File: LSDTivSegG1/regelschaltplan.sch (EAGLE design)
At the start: 47 parts, among them IC3 MAX232, IC4 MEGA32-P, Q2 BSS101, Q3 BSS101, Q4 BSS101, Q5 BSS101, Q6 BSS101, Q7 BSS101, Q8 BSS101, Q9 BSS101

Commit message: edit new schaltplan
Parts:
- removed IC3/7803: (no value), v-reg:78XXS
- added C12, C13, C14, C15, C16, C17: 100n, rcl:C-EU025-025X050
- added IC1: LF33AB, lsd2016:LF33AB
- added JP1: (no value), jumper:JP1E
- added R10: 10K, rcl:R-EU_0207/7
- added R11: 10k, rcl:R-EU_0207/7
- added R12, R13, R14: 240, rcl:R-EU_0207/7
- added SJ1, SJ2, SJ3, SJ4, SJ5, SJ6, SJ7, SJ8: (no value), jumper:SJ
- added SV1: (no value), con-lstb:MA05-2
- C1, C2: value (none) -> 15p
- C10, C11, C8, C9: value (none) -> 1u
- C3, C4, C6, C7: value (none) -> 100n
- C5: value (none) -> 1000u
- R1, R2, R3, R4, R5, R6, R7, R8: value (none) -> 240; device rcl:R-EU_0204/7 -> rcl:R-EU_0207/7
- R9: value (none) -> 10K; device rcl:R-EU_0204/7 -> rcl:R-EU_0207/7
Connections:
- new net ACCEL_X: C16.1, IC4.(ADC4)PA4, U$3.ACCEL_X
- new net ACCEL_Y: C17.1, IC4.(ADC3)PA3, U$3.ACCEL_Y
- new net FOOT_SW_B: IC4.(TOSC2)PC7, R11.2, U$2.FOOT_SW_B
- new net GYRO_REF: C15.1, IC4.(ADC5)PA5, U$3.GYRO_REF
- new net GYRO_X: C13.1, IC4.(ADC7)PA7, U$3.GYRO_X
- new net GYRO_Y: C14.1, IC4.(ADC6)PA6, U$3.GYRO_Y
- new net MISO: IC4.(MISO)PB6, SV1.9
- new net MOSI: IC4.(MOSI)PB5, SV1.1
- new net N$19: Q9.D, SJ8.1
- new net N$30: Q8.D, SJ7.1
- new net N$31: Q7.D, SJ6.1
- new net N$34: Q4.D, SJ3.1
- new net N$35: Q3.D, SJ2.1
- new net N$45: JP1.2, X1.9
- new net N$46: LED1.C, R3.1
- new net N$47: C5.1, IC4.(OC2)PD7, R10.1
- new net POTI: C12.1, IC4.(ADC1)PA1, U$2.POTI_CONTACT
- new net RESET: C6.2, IC4.RESET, R9.2, SV1.5
- new net SCK: IC4.(SCK)PB7, SV1.7
- new net STATUS_LED1: IC4.(T1)PB1, LED1.A
- new net STATUS_LED2: IC4.(AIN0/INT2)PB2, LED2.A
- new net STATUS_LED3: IC4.(AIN1/OC0)PB3, LED3.A
- net +3V3: now also IC1.OUT, Q9.G; no longer IC3/7803.OUT
- net +5V: now also IC1.IN, JP1.1, Q8.G, SJ1.2, SJ2.2, SJ3.2, SJ4.2, SJ5.2, SJ6.2, SJ7.2, SJ8.2, SV1.2; no longer IC3/7803.IN, Q2.D, Q3.D, Q4.D, Q5.D, Q6.D, Q7.D, Q8.D, Q9.D, X1.9
- net BAT_PWM: now also Q7.G, R10.2
- net DIROUT_1: now also IC4.(ICP)PD6, Q4.G
- net DIROUT_2: now also IC4.(INT1)PD3, Q5.G
- net ENABLE: now also IC4.(TCK)PC2, IC4.(TDO)PC4, Q6.G
- net GND: now also C12.2, C13.2, C14.2, C15.2, C16.2, C17.2, C5.2, IC1.GND, R1.2, R11.1, R12.2, R13.2, R14.2, R2.2, R3.2, R4.2, R5.2, R6.2, R7.2, R8.2, SV1.10, SV1.4, SV1.6, SV1.8; no longer IC3/7803.GND, LED1.C, LED2.C, LED3.C, R1.1, R2.1, R3.1, R4.1, R5.1, R6.1, R7.1, R8.1
- net MOTOR_PWM1: now also IC4.(OC1A)PD5, Q2.G
- net MOTOR_PWM2: now also IC4.(OC1B)PD4, Q3.G
- net N$10: now also R5.1; no longer R2.2
- net N$11: now also R6.1; no longer R3.2
- net N$14: now also R7.1; no longer R4.2
- net N$15: now also R8.1; no longer R5.2
- net N$16: now also R12.1; no longer R6.2
- net N$17: now also R13.1; no longer R7.2
- net N$18: now also R14.1; no longer R8.2
- net N$28: now also LED2.C, R2.1; no longer U$2.FOOT_SW_B
- net N$29: now also LED3.C, R1.1; no longer U$2.POTI_CONTACT
- net N$32: now also Q6.D, SJ5.1; no longer X1.3
- net N$33: now also Q5.D, SJ4.1; no longer X1.4
- net N$4: now also Q2.D, SJ1.1; no longer C6.2, IC4.RESET
- net N$7: now also R4.1; no longer R1.2
- net RS232RX: now also X1.3
- net RS232TX: now also X1.4
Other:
- moved on the sheet: C5, LEISTUNG-10, LEISTUNG-2, LEISTUNG-4, LEISTUNG-6, LEISTUNG-8, Q2, Q4, Q6, Q8, R1, R2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

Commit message: moved decoupling to regelungsplatine
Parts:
- added DC1: TMR, traco_tmr:TMR
- added IC10, IC11: LTV844, lsd2016:LTV844
- added LED12: blau, led:LED3MM
- added R15, R16, R17, R25, R26, R27: 220, rcl:R-EU_0207/10
- added R28, R29, R30, R31, R32, R33: 10k, rcl:R-EU_0207/10
- added R34: 100, rcl:R-EU_0207/10
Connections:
- net N$13 renamed NC
- removed net BAT_PWM: LEISTUNG-6.S, Q7.G, R10.2
- removed net DIROUT_1: IC4.(ICP)PD6, LEISTUNG-5.S, Q4.G
- removed net DIROUT_2: IC4.(INT1)PD3, LEISTUNG-7.S, Q5.G
- removed net ENABLE: IC4.(TCK)PC2, IC4.(TDO)PC4, LEISTUNG-9.S, Q6.G
- removed net MOTOR_PWM1: IC4.(OC1A)PD5, LEISTUNG-2.S, Q2.G
- removed net MOTOR_PWM2: IC4.(OC1B)PD4, LEISTUNG-4.S, Q3.G
- removed net N$12: LEISTUNG-8.S
- new net +24V: DC1.+VIN, LEISTUNG-1.S
- new net 5V_LST: LEISTUNG-8.S, R28.1, R29.1, R30.1, R32.1, R33.1
- new net BAT_-: DC1.-VIN, IC10G$1.EMIT, IC10G$2.EMIT, IC10G$3.EMIT, IC10G$4.C, IC11G$1.EMIT, IC11G$2.EMIT, LEISTUNG-3.S
- new net BAT_PWM_CTL: IC10G$4.COL, Q7.G, R10.2, R31.2
- new net BAT_PWM_LST: LEISTUNG-6.S, R25.1
- new net DIRL_CTL: IC4.(ICP)PD6, Q4.G, R15.1
- new net DIRL_LST: IC10G$1.COL, LEISTUNG-5.S, R28.2
- new net DIRR_CTL: IC4.(INT1)PD3, Q5.G, R16.1
- new net DIRR_LST: IC10G$2.COL, LEISTUNG-7.S, R29.2
- new net ENABLE_CTL: IC4.(TCK)PC2, IC4.(TDO)PC4, Q6.G, R17.1
- new net ENABLE_LST: IC10G$3.COL, LEISTUNG-9.S, R30.2
- new net MOTOR_PWM_LST: LEISTUNG-2.S, LEISTUNG-4.S
- new net MOTOR_PWM_L_CTL: IC4.(OC1A)PD5, Q2.G, R26.1
- new net MOTOR_PWM_L_LST: IC11G$1.COL, R32.2
- new net MOTOR_PWM_R_CTL: IC4.(OC1B)PD4, Q3.G, R27.1
- new net MOTOR_PWM_R_LST: IC11G$2.COL, R33.2
- new net N$36: IC10G$1.A, R15.2
- new net N$37: IC10G$2.A, R16.2
- new net N$38: IC10G$3.A, R17.2
- new net N$39: IC10G$4.A, R25.2
- new net N$40: IC11G$2.A, R27.2
- new net N$41: IC11G$1.A, R26.2
- new net N$42: LED12.A, R34.1
- net +5V: now also DC1.+VOUT, R31.1, R34.2; no longer LEISTUNG-1.S
- net GND: now also C11.+, DC1.-VOUT, IC10G$1.C, IC10G$2.C, IC10G$3.C, IC10G$4.EMIT, IC11G$1.C, IC11G$2.C, LED12.C; no longer C11.-, LEISTUNG-3.S
- net N$9: now also C11.-; no longer C11.+
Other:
- note added: "CTL"
- note added: "DCDC Converter"
- note added: "LST"
- note added: "On/Off NC for On State"
- note added: "Optocouplers"

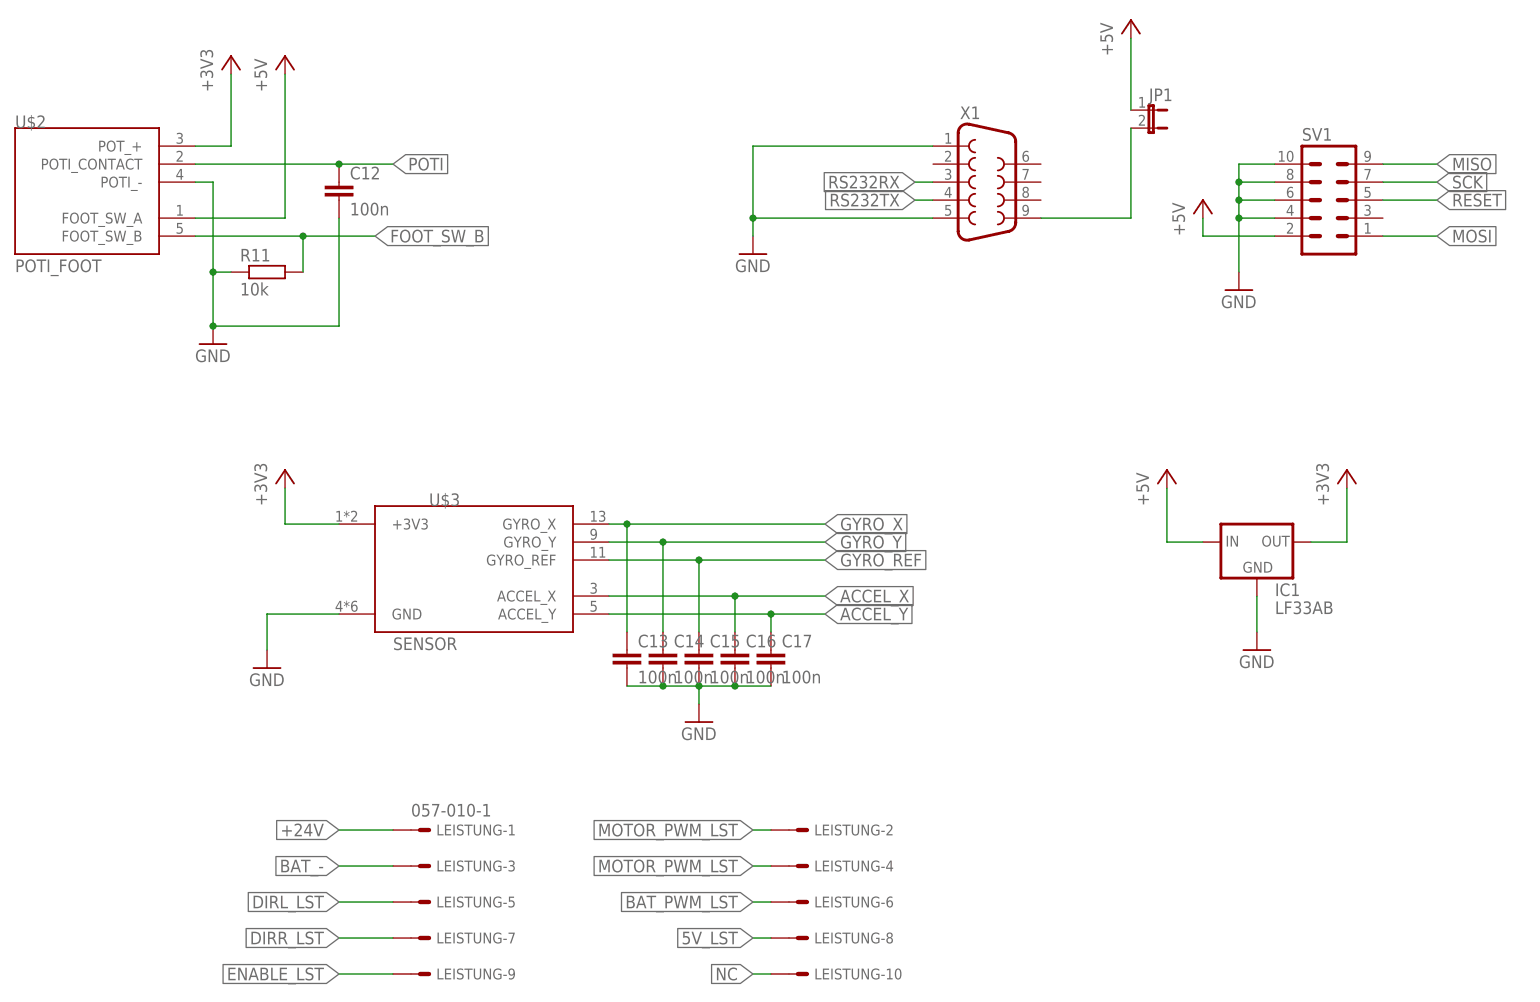
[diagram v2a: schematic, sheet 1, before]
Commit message: added blocking capacitors to 3V3 supply added rs323 cross pinhead
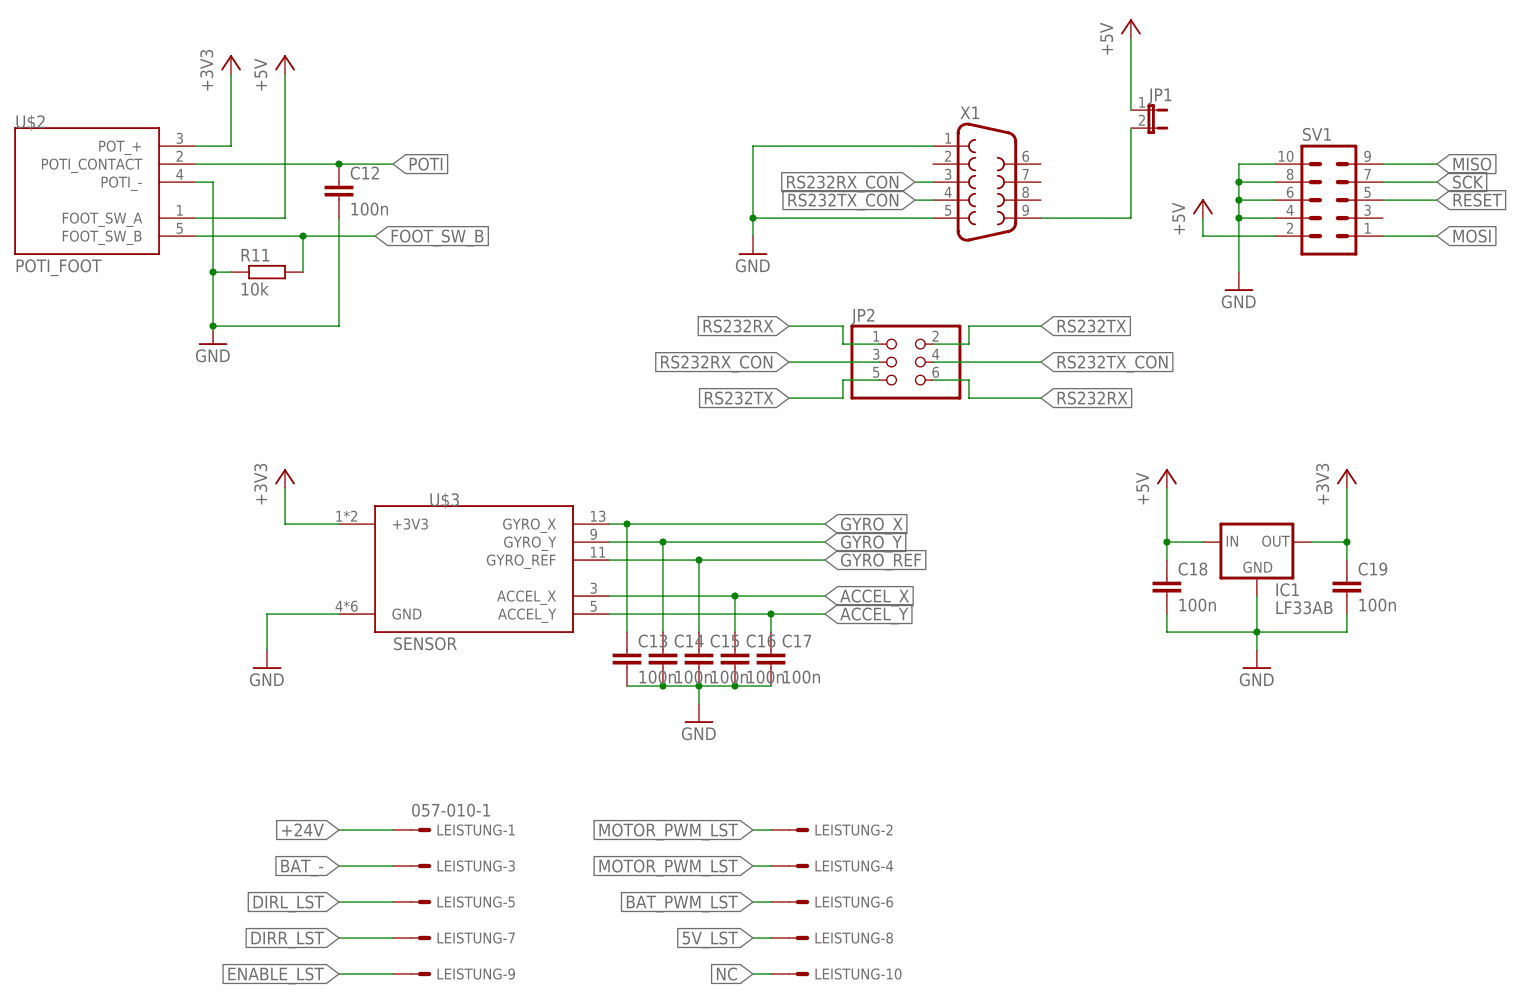
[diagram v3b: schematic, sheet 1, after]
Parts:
- added C18, C19: 100n, rcl:C-EU025-025X050
- added JP2: (no value), pinhead:PINHD-2X3
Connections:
- new net RS232RX_CON: JP2.3, X1.3
- new net RS232TX_CON: JP2.4, X1.4
- net +3V3: now also C19.1
- net +5V: now also C18.1
- net GND: now also C18.2, C19.2
- net RS232RX: now also JP2.1, JP2.6; no longer X1.3
- net RS232TX: now also JP2.2, JP2.5; no longer X1.4
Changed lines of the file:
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@@
 <part name="GND14" library="supply1" library_urn="urn:adsk.eagle:library:371" deviceset="GND" device=""/>
 <part name="GND15" library="supply1" library_urn="urn:adsk.eagle:library:371" deviceset="GND" device=""/>
+<part name="C18" library="rcl" deviceset="C-EU" device="025-025X050" value="100n"/>
+<part name="C19" library="rcl" deviceset="C-EU" device="025-025X050" value="100n"/>
+<part name="JP2" library="pinhead" library_urn="urn:adsk.eagle:library:325" deviceset="PINHD-2X3" device="" package3d_urn="urn:adsk.eagle:package:22462/2"/>
 </parts>
 <sheets>
@@
 <instance part="P+6" gate="1" x="83.82" y="60.96"/>
 <instance part="+3V2" gate="G$1" x="109.22" y="60.96"/>
-<instance part="GND4" gate="1" x="96.52" y="35.56"/>
+<instance part="GND4" gate="1" x="96.52" y="33.02"/>
 <instance part="GND5" gate="1" x="-43.18" y="33.02"/>
 <instance part="GND6" gate="1" x="-50.8" y="78.74"/>
@@
 <instance part="JP1" gate="A" x="81.28" y="111.76" rot="R270"/>
 <instance part="R11" gate="G$1" x="-43.18" y="88.9"/>
+<instance part="C18" gate="G$1" x="83.82" y="45.72"/>
+<instance part="C19" gate="G$1" x="109.22" y="45.72"/>
+<instance part="JP2" gate="A" x="45.72" y="76.2"/>
 </instances>
 <busses>
@@
 <wire x1="83.82" y1="50.8" x2="83.82" y2="58.42" width="0.1524" layer="91"/>
 <pinref part="IC1" gate="G$1" pin="IN"/>
+<pinref part="C18" gate="G$1" pin="1"/>
+<wire x1="83.82" y1="50.8" x2="83.82" y2="48.26" width="0.1524" layer="91"/>
+<junction x="83.82" y="50.8"/>
 </segment>
 <segment>
@@
 <segment>
 <pinref part="GND4" gate="1" pin="GND"/>
+<wire x1="96.52" y1="35.56" x2="96.52" y2="38.1" width="0.1524" layer="91"/>
+<pinref part="IC1" gate="G$1" pin="GND"/>
+<pinref part="C18" gate="G$1" pin="2"/>
 <wire x1="96.52" y1="38.1" x2="96.52" y2="43.18" width="0.1524" layer="91"/>
-<pinref part="IC1" gate="G$1" pin="GND"/>
+<wire x1="83.82" y1="40.64" x2="83.82" y2="38.1" width="0.1524" layer="91"/>
+<wire x1="83.82" y1="38.1" x2="96.52" y2="38.1" width="0.1524" layer="91"/>
+<junction x="96.52" y="38.1"/>
+<pinref part="C19" gate="G$1" pin="2"/>
+<wire x1="109.22" y1="38.1" x2="109.22" y2="40.64" width="0.1524" layer="91"/>
+<wire x1="109.22" y1="38.1" x2="96.52" y2="38.1" width="0.1524" layer="91"/>
 </segment>
 <segment>
@@
 <wire x1="109.22" y1="50.8" x2="104.14" y2="50.8" width="0.1524" layer="91"/>
 <pinref part="IC1" gate="G$1" pin="OUT"/>
+<pinref part="C19" gate="G$1" pin="1"/>
+<wire x1="109.22" y1="50.8" x2="109.22" y2="48.26" width="0.1524" layer="91"/>
+<junction x="109.22" y="50.8"/>
 </segment>
 <segment>
@@
 </segment>
 </net>
-<net name="RS232RX" class="0">
-<segment>
-<pinref part="X1" gate="G$1" pin="3"/>
-<wire x1="50.8" y1="101.6" x2="48.26" y2="101.6" width="0.1524" layer="91"/>
-<label x="48.26" y="101.6" size="1.778" layer="95" rot="R180" xref="yes"/>
-</segment>
-</net>
-<net name="RS232TX" class="0">
-<segment>
-<pinref part="X1" gate="G$1" pin="4"/>
-<wire x1="50.8" y1="99.06" x2="48.26" y2="99.06" width="0.1524" layer="91"/>
-<label x="48.26" y="99.06" size="1.778" layer="95" rot="R180" xref="yes"/>
-</segment>
-</net>
 <net name="GYRO_X" class="0">
 <segment>
@@
 <wire x1="27.94" y1="0" x2="25.4" y2="0" width="0.1524" layer="91"/>
 <label x="25.4" y="0" size="1.778" layer="95" rot="R180" xref="yes"/>
+</segment>
+</net>
+<net name="RS232TX_CON" class="0">
+<segment>
+<pinref part="JP2" gate="A" pin="4"/>
+<wire x1="50.8" y1="76.2" x2="66.04" y2="76.2" width="0.1524" layer="91"/>
+<label x="66.04" y="76.2" size="1.778" layer="95" xref="yes"/>
+</segment>
+<segment>
+<pinref part="X1" gate="G$1" pin="4"/>
+<wire x1="50.8" y1="99.06" x2="48.26" y2="99.06" width="0.1524" layer="91"/>
+<label x="48.26" y="99.06" size="1.778" layer="95" rot="R180" xref="yes"/>
+</segment>
+</net>
+<net name="RS232RX_CON" class="0">
+<segment>
+<pinref part="JP2" gate="A" pin="3"/>
+<wire x1="43.18" y1="76.2" x2="30.48" y2="76.2" width="0.1524" layer="91"/>
+<label x="30.48" y="76.2" size="1.778" layer="95" rot="R180" xref="yes"/>
+</segment>
+<segment>
+<pinref part="X1" gate="G$1" pin="3"/>
+<wire x1="50.8" y1="101.6" x2="48.26" y2="101.6" width="0.1524" layer="91"/>
+<label x="48.26" y="101.6" size="1.778" layer="95" rot="R180" xref="yes"/>
+</segment>
+</net>
+<net name="RS232RX" class="0">
+<segment>
+<pinref part="JP2" gate="A" pin="6"/>
+<wire x1="50.8" y1="73.66" x2="55.88" y2="73.66" width="0.1524" layer="91"/>
+<wire x1="55.88" y1="73.66" x2="55.88" y2="71.12" width="0.1524" layer="91"/>
+<wire x1="55.88" y1="71.12" x2="66.04" y2="71.12" width="0.1524" layer="91"/>
+<label x="66.04" y="71.12" size="1.778" layer="95" xref="yes"/>
+</segment>
+<segment>
+<pinref part="JP2" gate="A" pin="1"/>
+<wire x1="43.18" y1="78.74" x2="38.1" y2="78.74" width="0.1524" layer="91"/>
+<wire x1="38.1" y1="78.74" x2="38.1" y2="81.28" width="0.1524" layer="91"/>
+<wire x1="38.1" y1="81.28" x2="30.48" y2="81.28" width="0.1524" layer="91"/>
+<label x="30.48" y="81.28" size="1.778" layer="95" rot="R180" xref="yes"/>
+</segment>
+</net>
+<net name="RS232TX" class="0">
+<segment>
+<pinref part="JP2" gate="A" pin="2"/>
+<wire x1="50.8" y1="78.74" x2="55.88" y2="78.74" width="0.1524" layer="91"/>
+<wire x1="55.88" y1="78.74" x2="55.88" y2="81.28" width="0.1524" layer="91"/>
+<wire x1="55.88" y1="81.28" x2="66.04" y2="81.28" width="0.1524" layer="91"/>
+<label x="66.04" y="81.28" size="1.778" layer="95" xref="yes"/>
+</segment>
+<segment>
+<pinref part="JP2" gate="A" pin="5"/>
+<wire x1="43.18" y1="73.66" x2="38.1" y2="73.66" width="0.1524" layer="91"/>
+<wire x1="38.1" y1="73.66" x2="38.1" y2="71.12" width="0.1524" layer="91"/>
+<wire x1="38.1" y1="71.12" x2="30.48" y2="71.12" width="0.1524" layer="91"/>
+<label x="30.48" y="71.12" size="1.778" layer="95" rot="R180" xref="yes"/>
 </segment>
 </net>
@@
 will not be understood (or retained) with this version.
 </note>
+<note version="8.3" severity="warning">
+Since Version 8.3, EAGLE supports the association of 3D packages
+with devices in libraries, schematics, and board files. Those 3D
+packages will not be understood (or retained) with this version.
+</note>
 </compatibility>

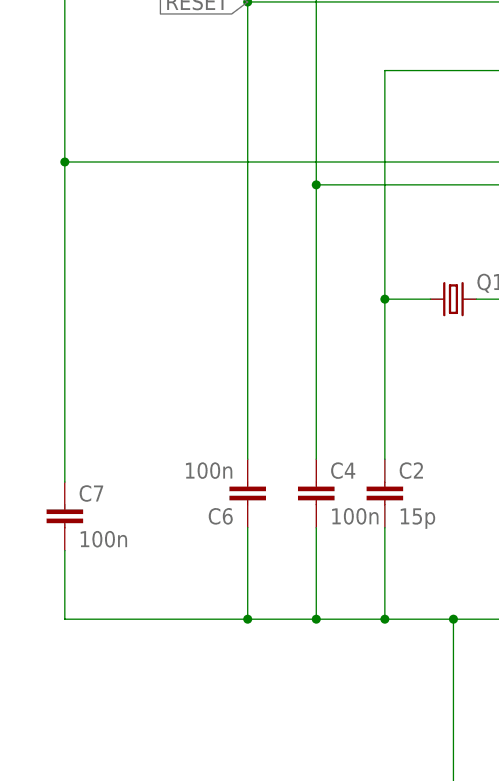
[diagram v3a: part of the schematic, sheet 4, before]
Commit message: fixed mirrored isp connector in display board
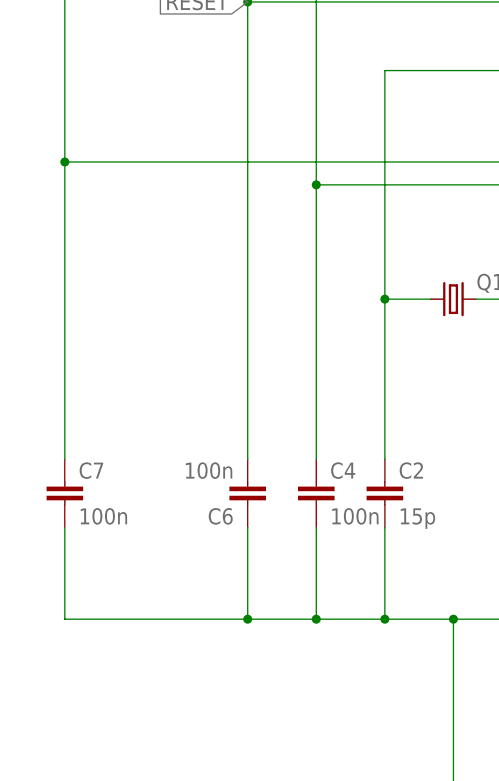
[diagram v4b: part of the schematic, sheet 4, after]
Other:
- moved on the sheet: C7
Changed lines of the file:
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@@
 <instance part="P+2" gate="1" x="-35.56" y="116.84"/>
 <instance part="+3V1" gate="G$1" x="-55.88" y="116.84"/>
-<instance part="C7" gate="G$1" x="-55.88" y="30.48"/>
+<instance part="C7" gate="G$1" x="-55.88" y="33.02"/>
 <instance part="FRAME1" gate="G$1" x="-93.98" y="-33.02"/>
 <instance part="GND7" gate="1" x="104.14" y="2.54"/>
@@
 <junction x="-27.94" y="17.78"/>
 <pinref part="C7" gate="G$1" pin="2"/>
-<wire x1="-55.88" y1="25.4" x2="-55.88" y2="17.78" width="0.1524" layer="91"/>
+<wire x1="-55.88" y1="27.94" x2="-55.88" y2="17.78" width="0.1524" layer="91"/>
 <wire x1="-55.88" y1="17.78" x2="-35.56" y2="17.78" width="0.1524" layer="91"/>
 <junction x="-35.56" y="17.78"/>
@@
 <pinref part="C7" gate="G$1" pin="1"/>
 <pinref part="IC4" gate="G$1" pin="AREF"/>
-<wire x1="-55.88" y1="68.58" x2="-55.88" y2="33.02" width="0.1524" layer="91"/>
+<wire x1="-55.88" y1="68.58" x2="-55.88" y2="35.56" width="0.1524" layer="91"/>
 <wire x1="15.24" y1="68.58" x2="-55.88" y2="68.58" width="0.1524" layer="91"/>
 <junction x="-55.88" y="68.58"/>
@@
 <pinref part="R27" gate="G$1" pin="1"/>
 <wire x1="165.1" y1="154.94" x2="162.56" y2="154.94" width="0.1524" layer="91"/>
-<label x="162.56" y="154.94" size="1.778" layer="95" rot="R180" xref="yes"/>
+<label x="162.56" y="154.94" size="1.27" layer="95" rot="R180" xref="yes"/>
 </segment>
 </net>
@@
 <pinref part="R26" gate="G$1" pin="1"/>
 <wire x1="165.1" y1="172.72" x2="162.56" y2="172.72" width="0.1524" layer="91"/>
-<label x="162.56" y="172.72" size="1.778" layer="95" rot="R180" xref="yes"/>
-</segment>
-</net>
+<label x="162.56" y="172.72" size="1.27" layer="95" rot="R180" xref="yes"/>
+</segment>
+</net>
